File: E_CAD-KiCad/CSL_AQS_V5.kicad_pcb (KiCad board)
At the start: 2 copper layers, 165.1 x 54.6 mm, 262 parts, among them J2 Grove STEMMA, J3 Grove STEMMA

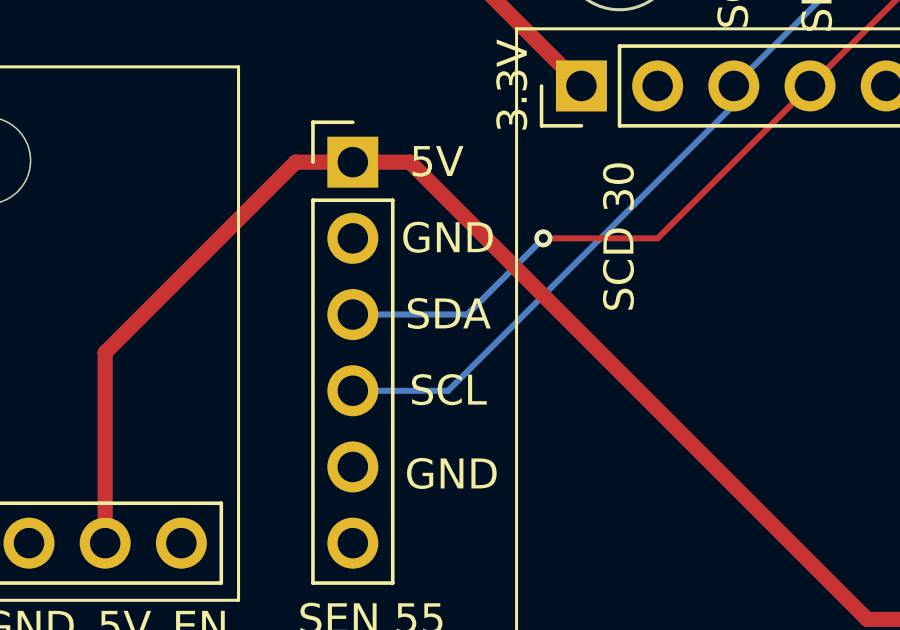
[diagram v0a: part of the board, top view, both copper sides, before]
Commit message: Reorganized E-CAD to updated version (5)
Updated to most recent version, version 5
Made updates to the schematic and PCB board in relation to SEN55
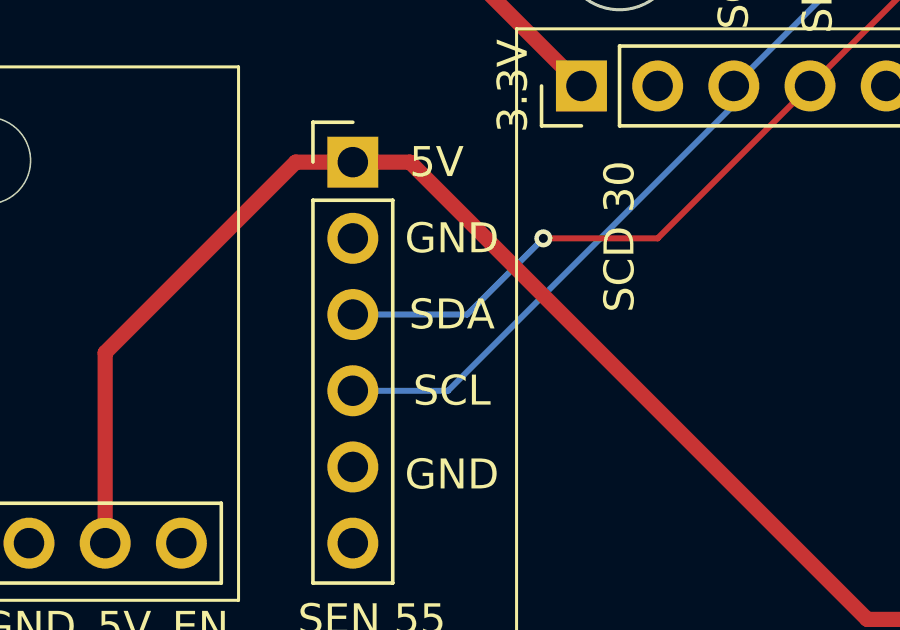
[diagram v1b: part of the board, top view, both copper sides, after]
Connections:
- A1 pad 1: Net-(A1-~{RESET}) -> unconnected-(A1-~{RESET}-Pad1)
- A1 pad 19: Net-(A1-D5) -> unconnected-(A1-D5-Pad19)
- A1 pad 20: Net-(A1-D6) -> unconnected-(A1-D6-Pad20)
- A1 pad 21: Net-(A1-D9) -> unconnected-(A1-D9-Pad21)
- A2 pad 1: Net-(A1-~{RESET}) -> unconnected-(A2-~{RESET}-Pad1)
- A2 pad 19: Net-(A1-D5) -> unconnected-(A2-D5-Pad19)
- A2 pad 20: Net-(A1-D6) -> unconnected-(A2-D6-Pad20)
- A2 pad 21: Net-(A1-D9) -> unconnected-(A2-D9-Pad21)
- JP8 pad 6: unconnected-(JP8-Pad6) -> NC
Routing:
- net (no net): track 0.00 -> 308.0 mm, vias 0 -> 5
- net Net-(A1-D9): track 86.8 -> 0.00 mm, vias 2 -> 0
- net Net-(A1-D6): track 86.4 -> 0.00 mm, vias 1 -> 0
- net Net-(A1-D5): track 83.7 -> 0.00 mm, vias 2 -> 0
- net Net-(A1-~{RESET}): track 51.1 -> 0.00 mm

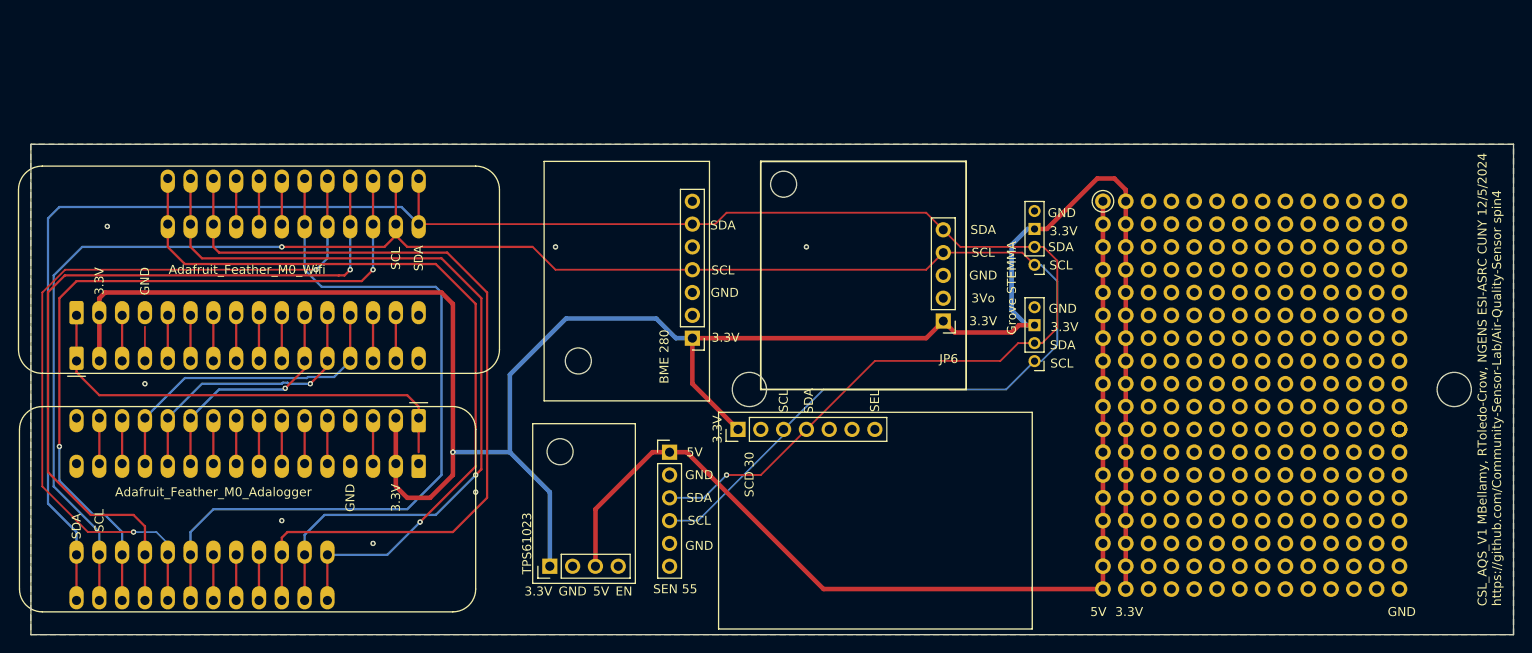
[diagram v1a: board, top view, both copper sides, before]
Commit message: Updated E-CAD File
Revisited a missed connection in the E-CAD files. Placement of the OLED when resetting should now function regardless of the board it is stacked on.
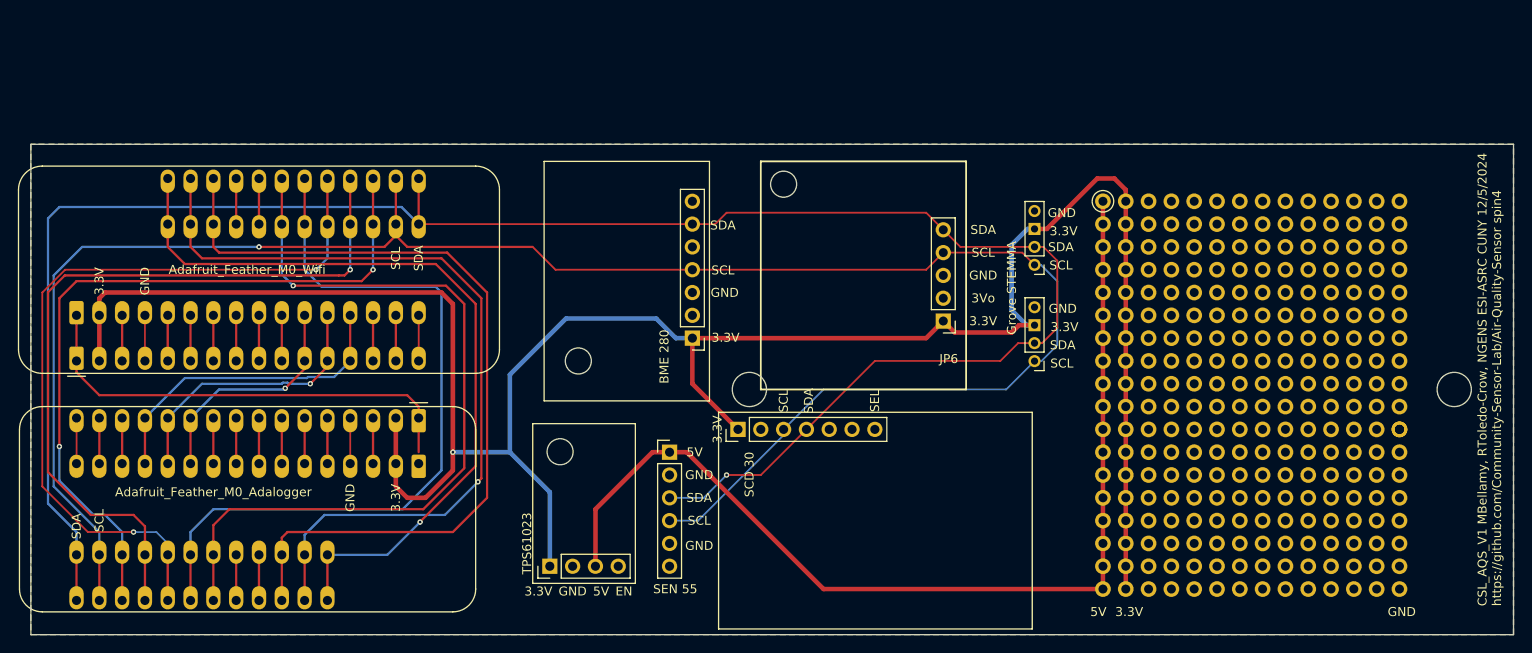
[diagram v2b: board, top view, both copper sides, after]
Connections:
- A1 pad 1: unconnected-(A1-~{RESET}-Pad1) -> Net-(A1-~{RESET})
- A2 pad 1: unconnected-(A2-~{RESET}-Pad1) -> Net-(A1-~{RESET})
- A2 pad 23: unconnected-(A2-D11-Pad23) -> ENA
- JP7 pad 5: NC -> unconnected-(JP7-Pad5)
- JP8 pad 6: NC -> unconnected-(JP8-Pad6)
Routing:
- net ENA: track 5.08 -> 89.6 mm, vias 0 -> 1
- net Net-(A1-~{RESET}): track 0.00 -> 51.1 mm
- net (no net): track 308.0 -> 256.9 mm
- net GND: track 4.25 -> 15.2 mm, vias 7 -> 0
- net unconnected-(A1-WAKE-Pad16): track 0.00 -> 5.08 mm
- net unconnected-(A2-D11-Pad23): track 5.08 -> 0.00 mm
- net Net-(A1-EN): track 91.4 -> 92.0 mm
